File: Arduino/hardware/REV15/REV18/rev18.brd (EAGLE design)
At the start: 50 x 50 mm, 6 parts, among them IC1 DS1820

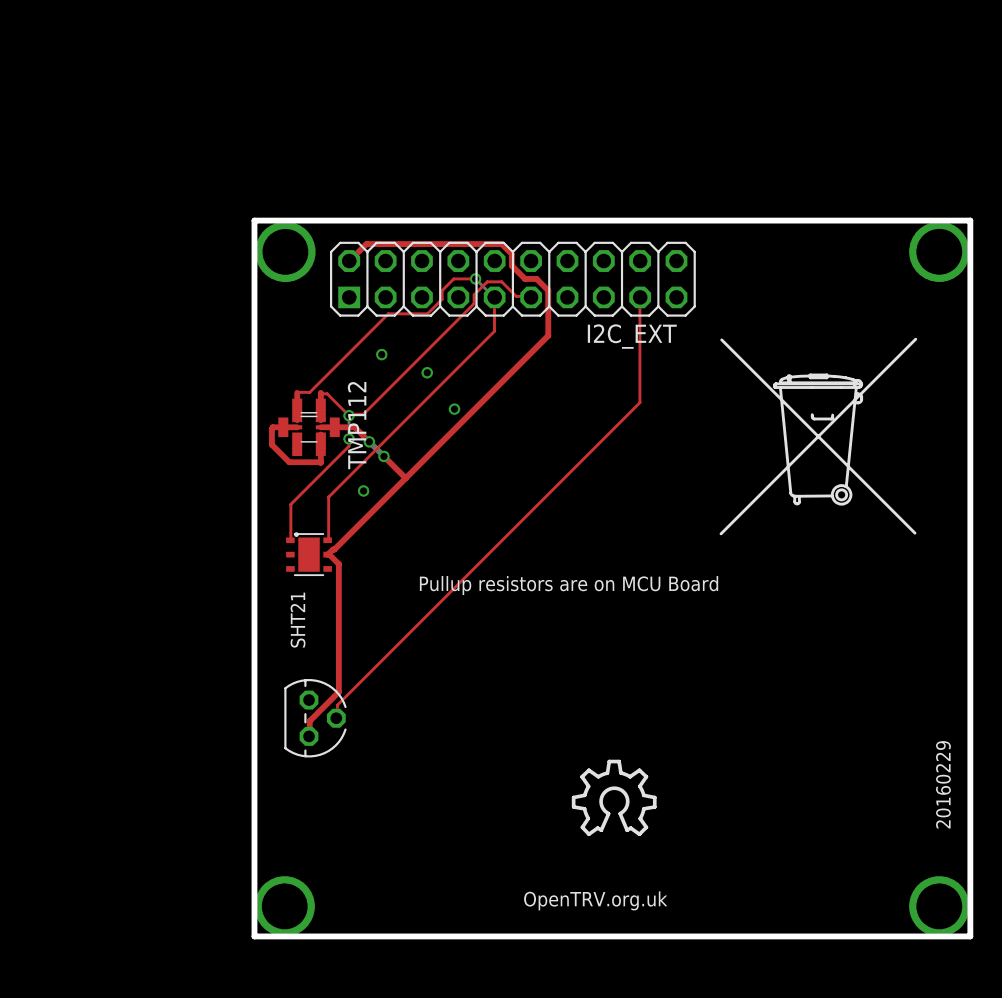
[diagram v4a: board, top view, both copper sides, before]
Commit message: rev15-18 changed as per Deniz suggeastions
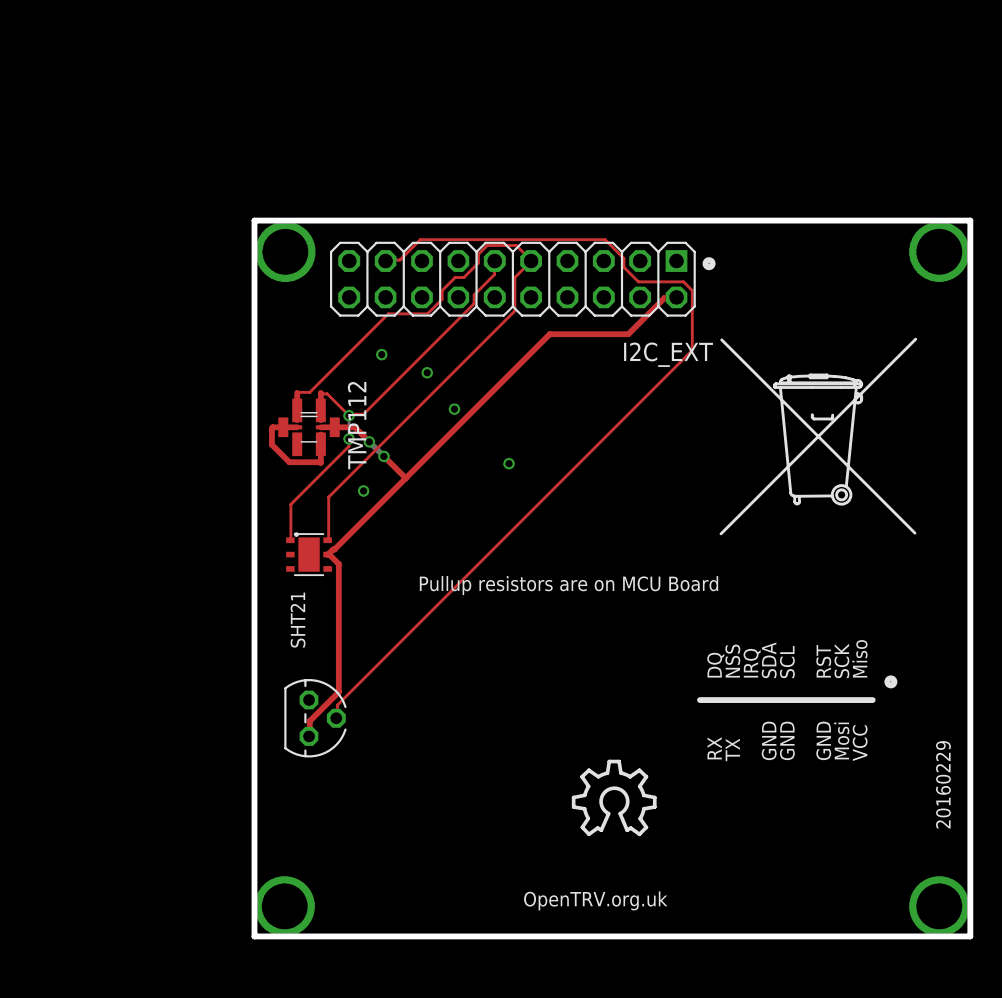
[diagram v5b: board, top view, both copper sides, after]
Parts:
- turned I2C_EXT to 180 degrees
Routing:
- net DQ: track 38.2 -> 64.1 mm
- net VCC: track 62.5 -> 53.2 mm
- net SCL: track 41.7 -> 49.1 mm, vias 1 -> 0
- net SDA: track 32.4 -> 30.5 mm
- net GND: vias 8 -> 9
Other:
- board text added: "DQ"
- board text added: "GND"
- board text added: "IRQ"
- board text added: "Miso"
- board text added: "Mosi"
- board text added: "NSS"
- board text added: "RST"
- board text added: "RX"
- board text added: "SCK"
- board text added: "SCL"
- board text added: "SDA"
- board text added: "TX"
- board text added: "VCC"
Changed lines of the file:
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@@
 <wire x1="50" y1="0" x2="0" y2="0" width="0.4064" layer="20"/>
 <text x="11.43" y="24.13" size="1" layer="25">Pullup resistors are on MCU Board</text>
+<text x="32.64" y="17.96" size="1" layer="25" rot="R90">DQ</text>
+<text x="36.45" y="17.96" size="1" layer="25" rot="R90">SDA</text>
+<text x="42.8" y="17.96" size="1" layer="25" rot="R90">Miso</text>
+<text x="42.8" y="12.245" size="1" layer="25" rot="R90">VCC</text>
+<text x="41.53" y="17.96" size="1" layer="25" rot="R90">SCK</text>
+<text x="41.53" y="12.245" size="1" layer="25" rot="R90">Mosi</text>
+<text x="40.26" y="17.96" size="1" layer="25" rot="R90">RST</text>
+<text x="40.26" y="12.245" size="1" layer="25" rot="R90">GND</text>
+<text x="35.18" y="17.96" size="1" layer="25" rot="R90">IRQ</text>
+<text x="33.91" y="17.96" size="1" layer="25" rot="R90">NSS</text>
+<text x="32.64" y="12.245" size="1" layer="25" rot="R90">RX</text>
+<text x="37.72" y="17.96" size="1" layer="25" rot="R90">SCL</text>
+<text x="33.91" y="12.245" size="1" layer="25" rot="R90">TX</text>
+<wire x1="43.18" y1="16.51" x2="31.115" y2="16.51" width="0.4064" layer="25"/>
+<text x="37.72" y="12.245" size="1" layer="25" rot="R90">GND</text>
+<text x="36.45" y="12.245" size="1" layer="25" rot="R90">GND</text>
+<circle x="44.45" y="17.78" radius="0.25" width="0.4064" layer="25"/>
+<circle x="31.75" y="46.99" radius="0.25" width="0.4064" layer="25"/>
 </plain>
 <attributes>
@@
 <element name="U$2" library="logo" package="TONNE" value="" x="39.235" y="32.16711875"/>
 <element name="U$1" library="ohw-logo" package="OSHW_10X200_NOTEXT" value="" x="22.294165625" y="7.13610625"/>
-<element name="I2C_EXT" library="pinhead" package="2X10" value="" x="18.05" y="45.905" smashed="yes">
-<attribute name="NAME" x="23.13" y="41.46" size="1.27" layer="25" ratio="10"/>
-<attribute name="VALUE" x="5.35" y="41.46" size="1.27" layer="27"/>
+<element name="I2C_EXT" library="pinhead" package="2X10" value="" x="18.05" y="45.905" smashed="yes" rot="R180">
+<attribute name="NAME" x="32.02" y="41.46" size="1.27" layer="25" ratio="10" rot="R180"/>
+<attribute name="VALUE" x="30.75" y="50.35" size="1.27" layer="27" rot="R180"/>
 </element>
 <element name="TMP112" library="TMP112_2" package="TMP112" value="TMP1" x="3.81" y="35.56" smashed="yes" rot="R270">
@@
 <wire x1="5.4864" y1="27.0256" x2="5.1816" y2="26.7208" width="0.4064" layer="1"/>
 <wire x1="5.588" y1="27.0256" x2="5.4864" y2="27.0256" width="0.4064" layer="1"/>
-<wire x1="20.5232" y1="41.9608" x2="10.5664" y2="32.004" width="0.4064" layer="1"/>
+<wire x1="20.6248" y1="42.0624" x2="10.5664" y2="32.004" width="0.4064" layer="1"/>
 <wire x1="10.5664" y1="32.004" x2="5.588" y2="27.0256" width="0.4064" layer="1"/>
-<wire x1="20.5232" y1="45.1104" x2="20.5232" y2="41.9608" width="0.4064" layer="1"/>
-<wire x1="19.7104" y1="45.9232" x2="20.5232" y2="45.1104" width="0.4064" layer="1"/>
-<wire x1="18.8976" y1="45.9232" x2="19.7104" y2="45.9232" width="0.4064" layer="1"/>
-<wire x1="17.9832" y1="46.8376" x2="18.8976" y2="45.9232" width="0.4064" layer="1"/>
-<wire x1="17.9832" y1="47.6504" x2="17.9832" y2="46.8376" width="0.4064" layer="1"/>
-<wire x1="17.272" y1="48.3616" x2="17.9832" y2="47.6504" width="0.4064" layer="1"/>
-<wire x1="7.8232" y1="48.3616" x2="17.272" y2="48.3616" width="0.4064" layer="1"/>
-<wire x1="6.7056" y1="47.244" x2="7.8232" y2="48.3616" width="0.4064" layer="1"/>
 <wire x1="5.1816" y1="26.7208" x2="5.11" y2="26.67" width="0.4064" layer="1"/>
-<wire x1="6.7056" y1="47.244" x2="6.62" y2="47.175" width="0.4064" layer="1"/>
 <wire x1="8.0264" y1="34.544" x2="7.0104" y2="35.56" width="0.4064" layer="1"/>
 <wire x1="9.0424" y1="33.528" x2="8.0264" y2="34.544" width="0.4064" layer="16"/>
@@
 <wire x1="3.8608" y1="14.0208" x2="3.81" y2="13.97" width="0.4064" layer="1"/>
 <wire x1="5.2832" y1="26.6192" x2="5.11" y2="26.67" width="0.4064" layer="1"/>
+<wire x1="28.6512" y1="44.6024" x2="29.464" y2="44.6024" width="0.4064" layer="1"/>
+<wire x1="26.1112" y1="42.0624" x2="28.6512" y2="44.6024" width="0.4064" layer="1"/>
+<wire x1="20.6248" y1="42.0624" x2="26.1112" y2="42.0624" width="0.4064" layer="1"/>
+<wire x1="29.464" y1="44.6024" x2="29.48" y2="44.635" width="0.4064" layer="1"/>
 </signal>
 <signal name="GND" class="1">
@@
 <via x="13.97" y="36.83" extent="1-16" drill="0.5"/>
 <via x="7.62" y="31.115" extent="1-16" drill="0.5"/>
+<via x="17.78" y="33.02" extent="1-16" drill="0.5"/>
 </signal>
 <signal name="32KHZ">
@@
 <wire x1="4.635" y1="37.8968" x2="5.08" y2="37.8968" width="0.2032" layer="1"/>
 <wire x1="2.54" y1="27.7368" x2="2.51" y2="27.67" width="0.2032" layer="1"/>
-<wire x1="18.288" y1="44.704" x2="19.304" y2="44.704" width="0.2032" layer="1"/>
-<wire x1="17.272" y1="45.72" x2="18.288" y2="44.704" width="0.2032" layer="1"/>
-<wire x1="16.256" y1="45.72" x2="17.272" y2="45.72" width="0.2032" layer="1"/>
-<wire x1="15.3416" y1="44.8056" x2="16.256" y2="45.72" width="0.2032" layer="1"/>
-<wire x1="15.3416" y1="44.196" x2="15.3416" y2="44.8056" width="0.2032" layer="1"/>
-<wire x1="7.62" y1="36.4744" x2="15.3416" y2="44.196" width="0.2032" layer="1"/>
 <wire x1="6.604" y1="36.4744" x2="7.62" y2="36.4744" width="0.2032" layer="1"/>
-<wire x1="19.304" y1="44.704" x2="19.32" y2="44.635" width="0.2032" layer="1"/>
 <wire x1="6.604" y1="36.4744" x2="6.604" y2="36.3728" width="0.2032" layer="1"/>
 <via x="6.604" y="34.7472" extent="1-16" drill="0.5"/>
 <via x="6.604" y="36.3728" extent="1-16" drill="0.5"/>
+<wire x1="16.764" y1="46.228" x2="16.764" y2="47.1424" width="0.2032" layer="1"/>
+<wire x1="15.3416" y1="44.8056" x2="16.764" y2="46.228" width="0.2032" layer="1"/>
+<wire x1="15.3416" y1="44.196" x2="15.3416" y2="44.8056" width="0.2032" layer="1"/>
+<wire x1="7.62" y1="36.4744" x2="15.3416" y2="44.196" width="0.2032" layer="1"/>
+<wire x1="16.764" y1="47.1424" x2="16.78" y2="47.175" width="0.2032" layer="1"/>
 </signal>
 <signal name="SCL">
@@
 <wire x1="2.985" y1="36.06" x2="2.985" y2="37.965" width="0.4064" layer="1"/>
 <wire x1="5.1816" y1="30.6832" x2="5.1816" y2="27.7368" width="0.2032" layer="1"/>
-<wire x1="16.764" y1="42.2656" x2="5.1816" y2="30.6832" width="0.2032" layer="1"/>
-<wire x1="16.764" y1="44.6024" x2="16.764" y2="42.2656" width="0.2032" layer="1"/>
 <wire x1="5.1816" y1="27.7368" x2="5.11" y2="27.67" width="0.2032" layer="1"/>
-<wire x1="16.764" y1="44.6024" x2="16.78" y2="44.635" width="0.2032" layer="1"/>
 <wire x1="3.8608" y1="37.9984" x2="3.1496" y2="37.9984" width="0.2032" layer="1"/>
+<wire x1="3.1496" y1="37.9984" x2="2.985" y2="37.965" width="0.2032" layer="1"/>
 <wire x1="9.3472" y1="43.4848" x2="3.8608" y2="37.9984" width="0.2032" layer="1"/>
 <wire x1="12.0904" y1="43.4848" x2="9.3472" y2="43.4848" width="0.2032" layer="1"/>
 <wire x1="13.1064" y1="44.5008" x2="12.0904" y2="43.4848" width="0.2032" layer="1"/>
 <wire x1="13.1064" y1="45.1104" x2="13.1064" y2="44.5008" width="0.2032" layer="1"/>
-<wire x1="13.9192" y1="45.9232" x2="13.1064" y2="45.1104" width="0.2032" layer="1"/>
-<wire x1="15.4432" y1="45.9232" x2="13.9192" y2="45.9232" width="0.2032" layer="1"/>
-<wire x1="16.764" y1="44.6024" x2="15.4432" y2="45.9232" width="0.2032" layer="16"/>
-<wire x1="3.1496" y1="37.9984" x2="2.985" y2="37.965" width="0.2032" layer="1"/>
-<wire x1="16.764" y1="44.6024" x2="16.78" y2="44.635" width="0.2032" layer="16"/>
-<via x="15.4432" y="45.9232" extent="1-16" drill="0.5"/>
+<wire x1="14.0208" y1="46.0248" x2="13.1064" y2="45.1104" width="0.2032" layer="1"/>
+<wire x1="14.6304" y1="46.0248" x2="14.0208" y2="46.0248" width="0.2032" layer="1"/>
+<wire x1="15.6464" y1="47.0408" x2="14.6304" y2="46.0248" width="0.2032" layer="1"/>
+<wire x1="15.6464" y1="47.6504" x2="15.6464" y2="47.0408" width="0.2032" layer="1"/>
+<wire x1="16.256" y1="48.26" x2="15.6464" y2="47.6504" width="0.2032" layer="1"/>
+<wire x1="18.288" y1="48.26" x2="16.256" y2="48.26" width="0.2032" layer="1"/>
+<wire x1="19.304" y1="47.244" x2="18.288" y2="48.26" width="0.2032" layer="1"/>
+<wire x1="19.304" y1="47.244" x2="19.32" y2="47.175" width="0.2032" layer="1"/>
+<wire x1="18.1864" y1="43.688" x2="5.1816" y2="30.6832" width="0.2032" layer="1"/>
+<wire x1="18.1864" y1="46.0248" x2="18.1864" y2="43.688" width="0.2032" layer="1"/>
+<wire x1="19.304" y1="47.1424" x2="18.1864" y2="46.0248" width="0.2032" layer="1"/>
+<wire x1="19.304" y1="47.1424" x2="19.32" y2="47.175" width="0.2032" layer="1"/>
 </signal>
 <signal name="DQ">
@@
 <contactref element="IC1" pad="2"/>
 <wire x1="5.7912" y1="16.1544" x2="5.7912" y2="15.24" width="0.2032" layer="1"/>
-<wire x1="26.924" y1="37.2872" x2="5.7912" y2="16.1544" width="0.2032" layer="1"/>
-<wire x1="26.924" y1="44.6024" x2="26.924" y2="37.2872" width="0.2032" layer="1"/>
+<wire x1="30.5816" y1="40.9448" x2="5.7912" y2="16.1544" width="0.2032" layer="1"/>
 <wire x1="5.7912" y1="15.24" x2="5.715" y2="15.24" width="0.2032" layer="1"/>
-<wire x1="26.924" y1="44.6024" x2="26.94" y2="44.635" width="0.2032" layer="1"/>
+<wire x1="10.16" y1="47.244" x2="9.2456" y2="47.244" width="0.2032" layer="1"/>
+<wire x1="11.5824" y1="48.6664" x2="10.16" y2="47.244" width="0.2032" layer="1"/>
+<wire x1="24.4856" y1="48.6664" x2="11.5824" y2="48.6664" width="0.2032" layer="1"/>
+<wire x1="25.8064" y1="47.3456" x2="24.4856" y2="48.6664" width="0.2032" layer="1"/>
+<wire x1="25.8064" y1="46.736" x2="25.8064" y2="47.3456" width="0.2032" layer="1"/>
+<wire x1="26.8224" y1="45.72" x2="25.8064" y2="46.736" width="0.2032" layer="1"/>
+<wire x1="29.972" y1="45.72" x2="26.8224" y2="45.72" width="0.2032" layer="1"/>
+<wire x1="30.5816" y1="45.1104" x2="29.972" y2="45.72" width="0.2032" layer="1"/>
+<wire x1="30.5816" y1="40.9448" x2="30.5816" y2="45.1104" width="0.2032" layer="1"/>
+<wire x1="9.2456" y1="47.244" x2="9.16" y2="47.175" width="0.2032" layer="1"/>
 </signal>
 </signals>

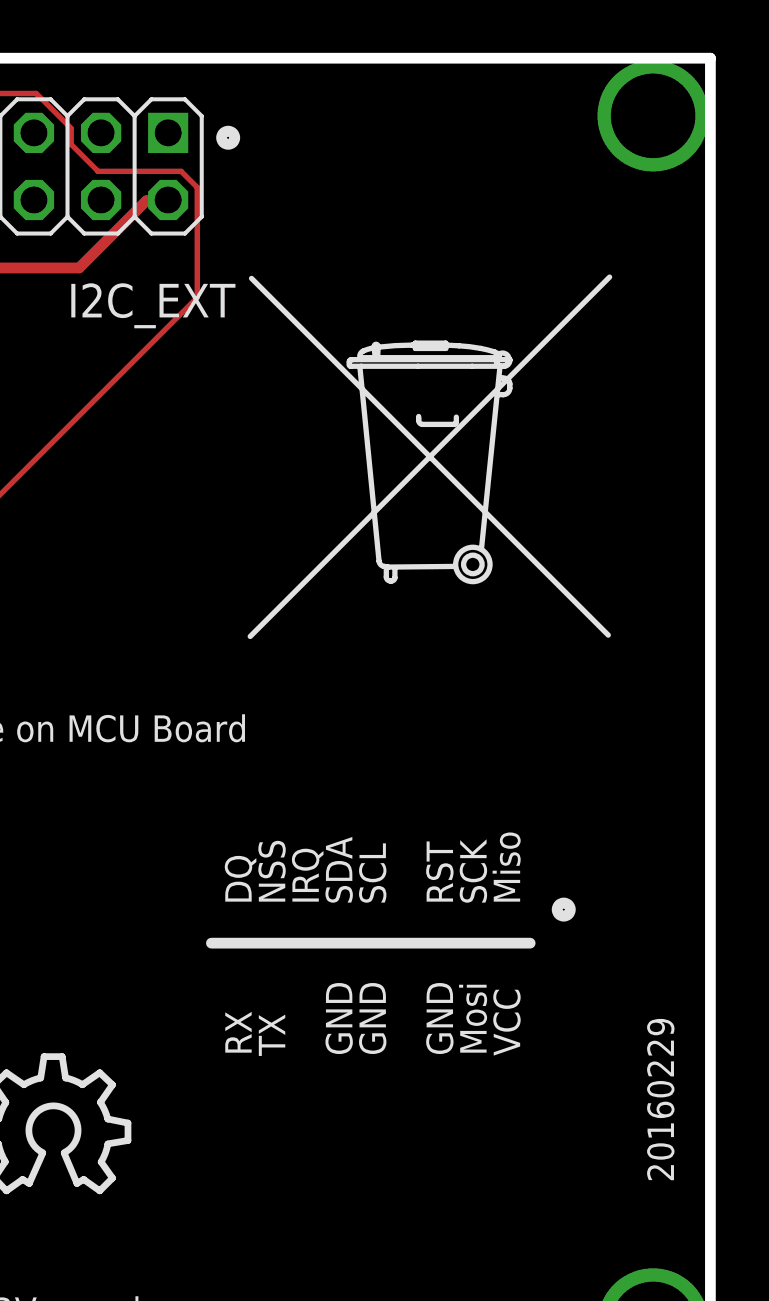
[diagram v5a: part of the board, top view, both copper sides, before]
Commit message: ic2_ext labels closer to connector
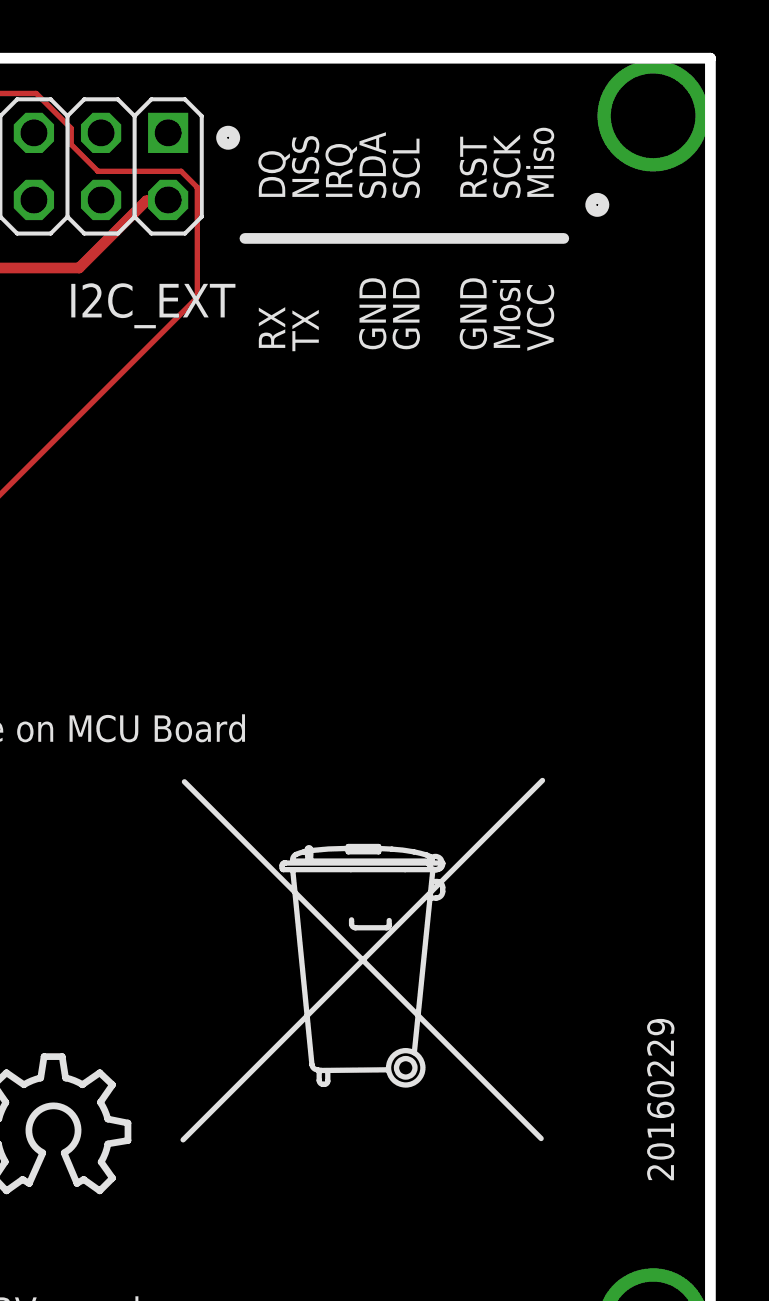
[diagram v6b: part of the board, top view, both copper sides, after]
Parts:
- moved U$2 19.2 mm to (36.7, 13.1)
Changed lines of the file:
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@@
 <wire x1="50" y1="0" x2="0" y2="0" width="0.4064" layer="20"/>
 <text x="11.43" y="24.13" size="1" layer="25">Pullup resistors are on MCU Board</text>
-<text x="32.64" y="17.96" size="1" layer="25" rot="R90">DQ</text>
-<text x="36.45" y="17.96" size="1" layer="25" rot="R90">SDA</text>
-<text x="42.8" y="17.96" size="1" layer="25" rot="R90">Miso</text>
-<text x="42.8" y="12.245" size="1" layer="25" rot="R90">VCC</text>
-<text x="41.53" y="17.96" size="1" layer="25" rot="R90">SCK</text>
-<text x="41.53" y="12.245" size="1" layer="25" rot="R90">Mosi</text>
-<text x="40.26" y="17.96" size="1" layer="25" rot="R90">RST</text>
-<text x="40.26" y="12.245" size="1" layer="25" rot="R90">GND</text>
-<text x="35.18" y="17.96" size="1" layer="25" rot="R90">IRQ</text>
-<text x="33.91" y="17.96" size="1" layer="25" rot="R90">NSS</text>
-<text x="32.64" y="12.245" size="1" layer="25" rot="R90">RX</text>
-<text x="37.72" y="17.96" size="1" layer="25" rot="R90">SCL</text>
-<text x="33.91" y="12.245" size="1" layer="25" rot="R90">TX</text>
-<wire x1="43.18" y1="16.51" x2="31.115" y2="16.51" width="0.4064" layer="25"/>
-<text x="37.72" y="12.245" size="1" layer="25" rot="R90">GND</text>
-<text x="36.45" y="12.245" size="1" layer="25" rot="R90">GND</text>
-<circle x="44.45" y="17.78" radius="0.25" width="0.4064" layer="25"/>
+<text x="33.91" y="44.63" size="1" layer="25" rot="R90">DQ</text>
+<text x="37.72" y="44.63" size="1" layer="25" rot="R90">SDA</text>
+<text x="44.07" y="44.63" size="1" layer="25" rot="R90">Miso</text>
+<text x="44.07" y="38.915" size="1" layer="25" rot="R90">VCC</text>
+<text x="42.8" y="44.63" size="1" layer="25" rot="R90">SCK</text>
+<text x="42.8" y="38.915" size="1" layer="25" rot="R90">Mosi</text>
+<text x="41.53" y="44.63" size="1" layer="25" rot="R90">RST</text>
+<text x="41.53" y="38.915" size="1" layer="25" rot="R90">GND</text>
+<text x="36.45" y="44.63" size="1" layer="25" rot="R90">IRQ</text>
+<text x="35.18" y="44.63" size="1" layer="25" rot="R90">NSS</text>
+<text x="33.91" y="38.915" size="1" layer="25" rot="R90">RX</text>
+<text x="38.99" y="44.63" size="1" layer="25" rot="R90">SCL</text>
+<text x="35.18" y="38.915" size="1" layer="25" rot="R90">TX</text>
+<wire x1="44.45" y1="43.18" x2="32.385" y2="43.18" width="0.4064" layer="25"/>
+<text x="38.99" y="38.915" size="1" layer="25" rot="R90">GND</text>
+<text x="37.72" y="38.915" size="1" layer="25" rot="R90">GND</text>
+<circle x="45.72" y="44.45" radius="0.25" width="0.4064" layer="25"/>
 <circle x="31.75" y="46.99" radius="0.25" width="0.4064" layer="25"/>
 </plain>
@@
 </autorouter>
 <elements>
-<element name="U$2" library="logo" package="TONNE" value="" x="39.235" y="32.16711875"/>
+<element name="U$2" library="logo" package="TONNE" value="" x="36.695" y="13.11711875"/>
 <element name="U$1" library="ohw-logo" package="OSHW_10X200_NOTEXT" value="" x="22.294165625" y="7.13610625"/>
 <element name="I2C_EXT" library="pinhead" package="2X10" value="" x="18.05" y="45.905" smashed="yes" rot="R180">
